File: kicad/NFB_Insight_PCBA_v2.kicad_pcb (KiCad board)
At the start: 4 copper layers, 242.3 x 68.6 mm, 120 parts

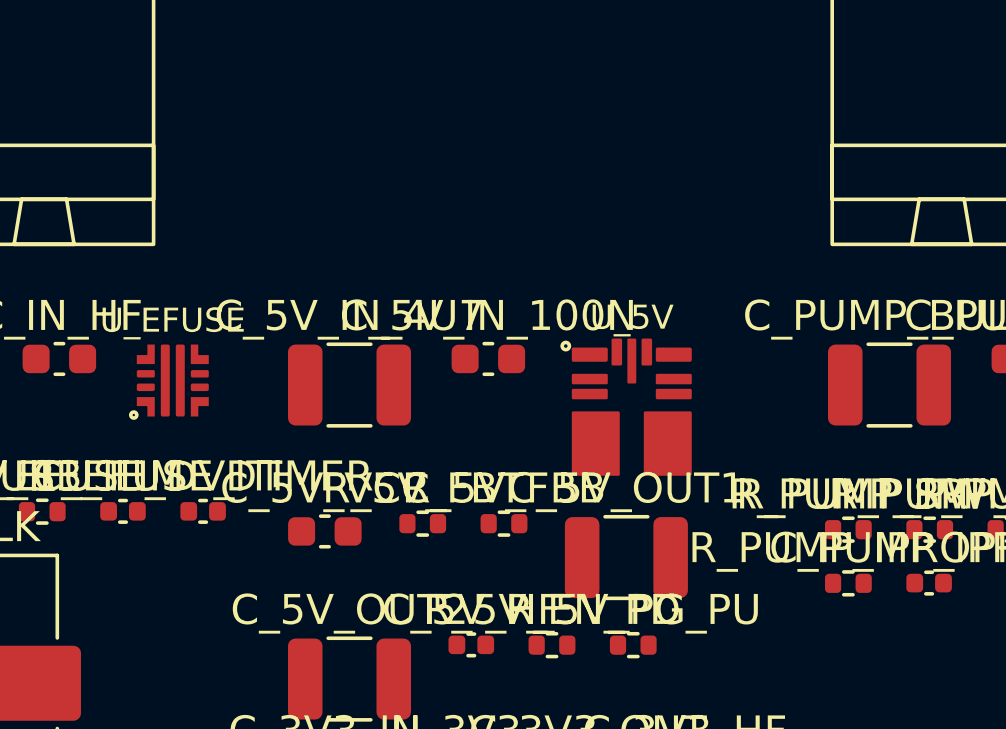
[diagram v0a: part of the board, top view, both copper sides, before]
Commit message: placement: corregir micro-isla TPSM33625 antes de routing
ECO local Z3 guiado por TI TPSM33625 §8.5.1. Mueve únicamente C_5V_IN_4U7, C_5V_IN_100N, C_5V_VCC, R_5V_FBT y R_5V_FBB; preserva U_5V, outline, zonas, netlist y routing. DRC físico=0; 114 refs restantes intactas. Integra reproducción semántica y conocimiento de ingeniería previo a reiniciar PR19A.
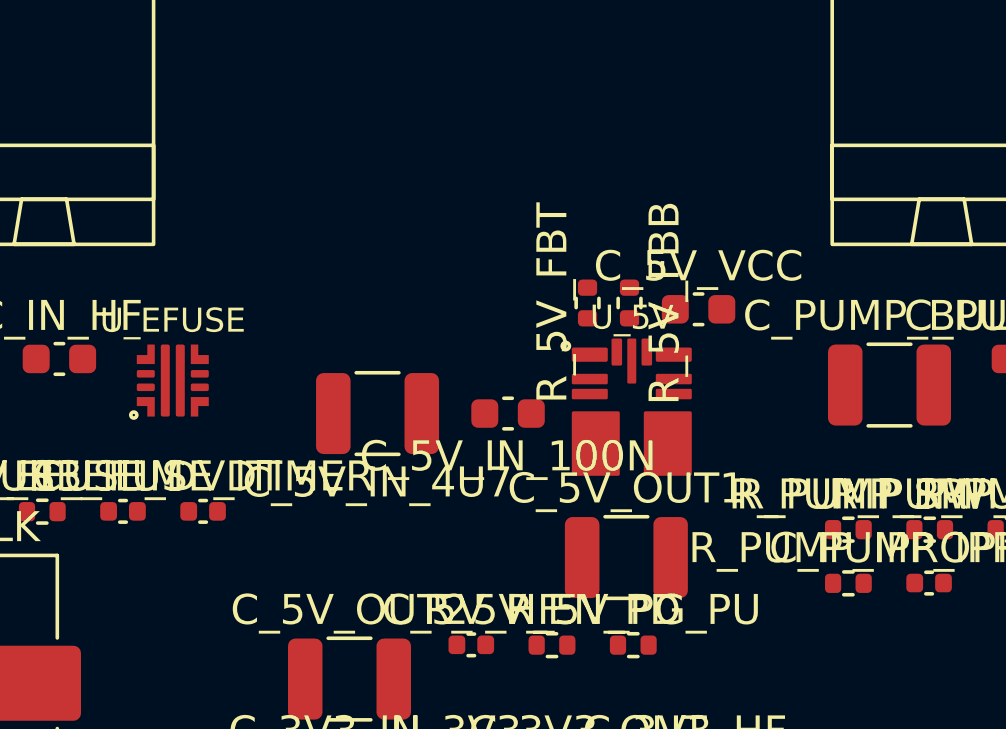
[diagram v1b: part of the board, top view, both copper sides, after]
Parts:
- moved C_5V_VCC 14.5 mm to (195.3, 15.6)
- moved R_5V_FBT 9.18 mm to (191.6, 15.4), turned to 90 degrees
- moved R_5V_FBB 8.46 mm to (193.0, 15.4), turned to -90 degrees
- moved C_5V_IN_100N 1.93 mm to (188.9, 19.1), turned to 180 degrees
- moved C_5V_IN_4U7 1.33 mm to (184.6, 19.1), turned to 180 degrees

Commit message: routing: persistir cobre PR19A 28/28 validado
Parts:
- moved TP_LOAD_A_NEG 35.5 mm to (112.8, 29.3)
- moved TP_LOAD_A_POS 35.3 mm to (110.2, 29.3)
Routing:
- net 5V_PGOOD: track 0.00 -> 68.9 mm
- net CO2_OPENLOAD_N: track 0.00 -> 54.2 mm, vias 0 -> 4
- net LOAD_A_POS: track 0.00 -> 51.9 mm, vias 0 -> 1
- net LOAD_A_NEG: track 0.00 -> 51.4 mm, vias 0 -> 2
- net WDT_MR_N: track 0.00 -> 47.7 mm
- net HMI_FIELD_TX: track 0.00 -> 30.6 mm, vias 0 -> 1
- net CO2_EN_DRV: track 0.00 -> 30.3 mm, vias 0 -> 2
- net HX_VBG: track 0.00 -> 25.6 mm
- net PUMP_SR_CFG: track 0.00 -> 24.2 mm, vias 0 -> 2
- net HMI_FIELD_RX: track 0.00 -> 24.1 mm
- net PH_FIELD_SIG: track 0.00 -> 22.6 mm
- net DO_FIELD_SIG: track 0.00 -> 21.6 mm
- net ORP_FIELD_SIG: track 0.00 -> 21.2 mm
- net CHILLER_CONTACT_B: track 0.00 -> 20.2 mm
- net CHILLER_CONTACT_A: track 0.00 -> 19.9 mm
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
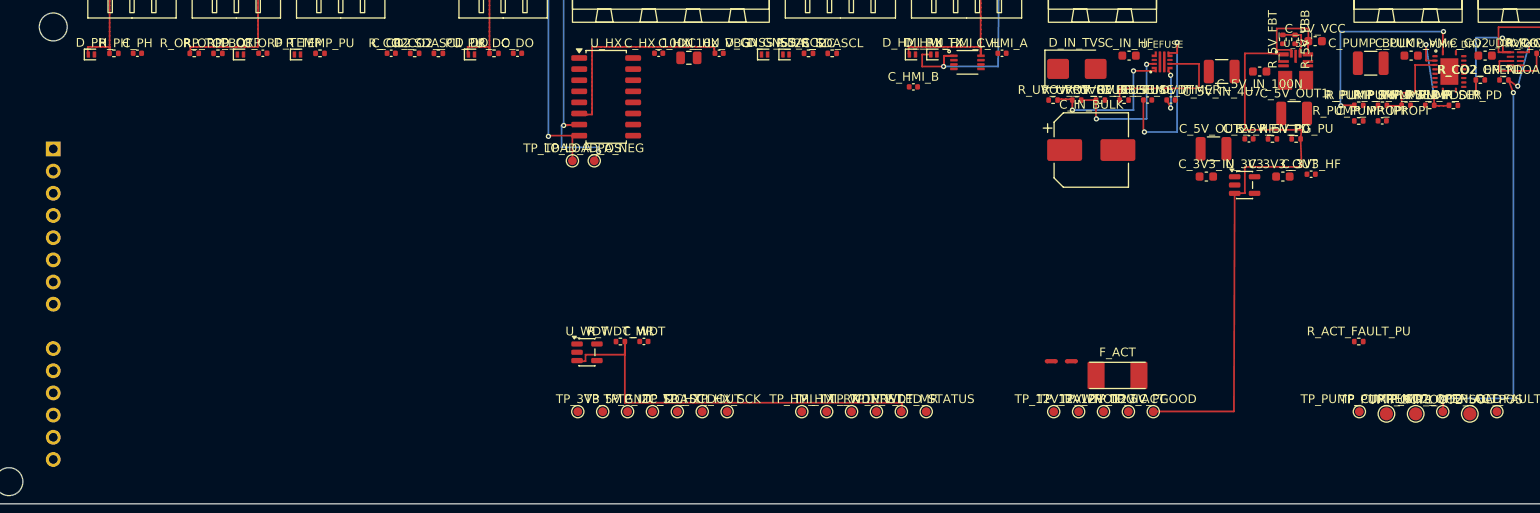
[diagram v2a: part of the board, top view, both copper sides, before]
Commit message: routing: persistir PR19B 4/4 DRC=0
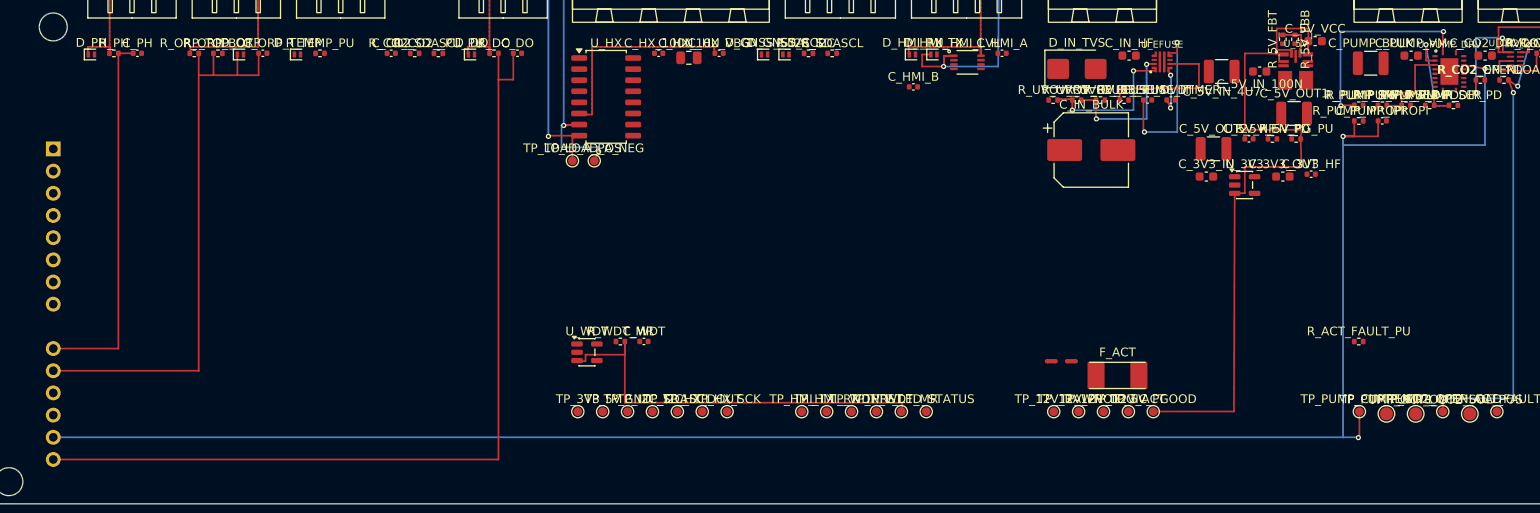
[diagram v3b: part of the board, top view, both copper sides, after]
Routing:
- net PUMP_CURRENT_ADC: track 0.00 -> 224.3 mm, vias 0 -> 3
- net DO_ADC: track 0.00 -> 102.2 mm
- net ORP_ADC: track 0.00 -> 67.3 mm
- net PH_ADC: track 0.00 -> 43.0 mm
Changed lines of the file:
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@@
 	)
 	(segment
+		(start 101.78 20)
+		(end 103.48 20)
+		(width 0.2)
+		(layer "F.Cu")
+		(net "DO_ADC")
+	)
+	(segment
+		(start 101.78 16.995)
+		(end 101.78 20)
+		(width 0.2)
+		(layer "F.Cu")
+		(net "DO_ADC")
+	)
+	(segment
+		(start 101.78 63.5)
+		(end 50.8 63.5)
+		(width 0.2)
+		(layer "F.Cu")
+		(net "DO_ADC")
+	)
+	(segment
+		(start 101.78 20)
+		(end 101.78 63.5)
+		(width 0.2)
+		(layer "F.Cu")
+		(net "DO_ADC")
+	)
+	(segment
+		(start 103.48 20)
+		(end 103.48 16.985)
+		(width 0.2)
+		(layer "F.Cu")
+		(net "DO_ADC")
+	)
+	(segment
 		(start 232.5 24.5)
 		(end 233.655 23.445)
@@
 	)
 	(segment
+		(start 199.785 26.5)
+		(end 198.5 26.5)
+		(width 0.2)
+		(layer "F.Cu")
+		(net "PUMP_CURRENT_ADC")
+	)
+	(segment
+		(start 202.505 26.5)
+		(end 198.5 26.5)
+		(width 0.2)
+		(layer "F.Cu")
+		(net "PUMP_CURRENT_ADC")
+	)
+	(segment
+		(start 199.785 24.735)
+		(end 199.785 26.5)
+		(width 0.2)
+		(layer "F.Cu")
+		(net "PUMP_CURRENT_ADC")
+	)
+	(segment
+		(start 200.365 60.96)
+		(end 200.365 58.025)
+		(width 0.2)
+		(layer "F.Cu")
+		(net "PUMP_CURRENT_ADC")
+	)
+	(segment
+		(start 202.505 24.725)
+		(end 202.505 26.5)
+		(width 0.2)
+		(layer "F.Cu")
+		(net "PUMP_CURRENT_ADC")
+	)
+	(segment
+		(start 212.325 18.325)
+		(end 214.75 18.75)
+		(width 0.2)
+		(layer "F.Cu")
+		(net "PUMP_CURRENT_ADC")
+	)
+	(via
+		(at 200.25 61)
+		(size 0.6)
+		(drill 0.3)
+		(layers "F.Cu" "B.Cu")
+		(net "PUMP_CURRENT_ADC")
+	)
+	(via
+		(at 214.75 18.75)
+		(size 0.6)
+		(drill 0.3)
+		(layers "F.Cu" "B.Cu")
+		(net "PUMP_CURRENT_ADC")
+	)
+	(via
+		(at 198.5 26.5)
+		(size 0.6)
+		(drill 0.3)
+		(layers "F.Cu" "B.Cu")
+		(net "PUMP_CURRENT_ADC")
+	)
+	(segment
+		(start 198.5 60.96)
+		(end 50.8 60.96)
+		(width 0.2)
+		(layer "B.Cu")
+		(net "PUMP_CURRENT_ADC")
+	)
+	(segment
+		(start 198.5 60.96)
+		(end 200.365 60.96)
+		(width 0.2)
+		(layer "B.Cu")
+		(net "PUMP_CURRENT_ADC")
+	)
+	(segment
+		(start 198.5 27.5)
+		(end 198.5 26.5)
+		(width 0.2)
+		(layer "B.Cu")
+		(net "PUMP_CURRENT_ADC")
+	)
+	(segment
+		(start 198.5 26.5)
+		(end 198.5 60.96)
+		(width 0.2)
+		(layer "B.Cu")
+		(net "PUMP_CURRENT_ADC")
+	)
+	(segment
+		(start 214.75 18.75)
+		(end 214.75 27.5)
+		(width 0.2)
+		(layer "B.Cu")
+		(net "PUMP_CURRENT_ADC")
+	)
+	(segment
+		(start 214.75 27.5)
+		(end 198.5 27.5)
+		(width 0.2)
+		(layer "B.Cu")
+		(net "PUMP_CURRENT_ADC")
+	)
+	(segment
+		(start 71.885 17.125)
+		(end 71.885 19.5)
+		(width 0.2)
+		(layer "F.Cu")
+		(net "ORP_ADC")
+	)
+	(segment
+		(start 74.315 16.985)
+		(end 74.315 19.5)
+		(width 0.2)
+		(layer "F.Cu")
+		(net "ORP_ADC")
+	)
+	(segment
+		(start 67.455 19.5)
+		(end 67.455 53.34)
+		(width 0.2)
+		(layer "F.Cu")
+		(net "ORP_ADC")
+	)
+	(segment
+		(start 67.455 19.5)
+		(end 74.315 19.5)
+		(width 0.2)
+		(layer "F.Cu")
+		(net "ORP_ADC")
+	)
+	(segment
+		(start 67.455 16.995)
+		(end 67.455 19.5)
+		(width 0.2)
+		(layer "F.Cu")
+		(net "ORP_ADC")
+	)
+	(segment
+		(start 69.145 16.995)
+		(end 69.145 19.5)
+		(width 0.2)
+		(layer "F.Cu")
+		(net "ORP_ADC")
+	)
+	(segment
+		(start 67.455 53.34)
+		(end 50.8 53.34)
+		(width 0.2)
+		(layer "F.Cu")
+		(net "ORP_ADC")
+	)
+	(segment
 		(start 225.2 16.995)
 		(end 224.395 16.995)
@@
 		(net "5V_FB")
 	)
+	(segment
+		(start 58.255 50.8)
+		(end 50.8 50.8)
+		(width 0.2)
+		(layer "F.Cu")
+		(net "PH_ADC")
+	)
+	(segment
+		(start 59.955 16.985)
+		(end 58.255 16.995)
+		(width 0.2)
+		(layer "F.Cu")
+		(net "PH_ADC")
+	)
+	(segment
+		(start 58.255 16.995)
+		(end 58.255 50.8)
+		(width 0.2)
+		(layer "F.Cu")
+		(net "PH_ADC")
+	)
 	(embedded_fonts no)
